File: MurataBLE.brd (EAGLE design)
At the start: 90 x 70 mm, 58 parts, among them CON1 47589-0001, IC2 LPC11U35_QFN33, IC3 NC7SZ00, IC4 AT25DN512C, IC5 AT25XE011, P1 NC, P2 NC, P3 NC, P4 NC, Q1 32.768K/2012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

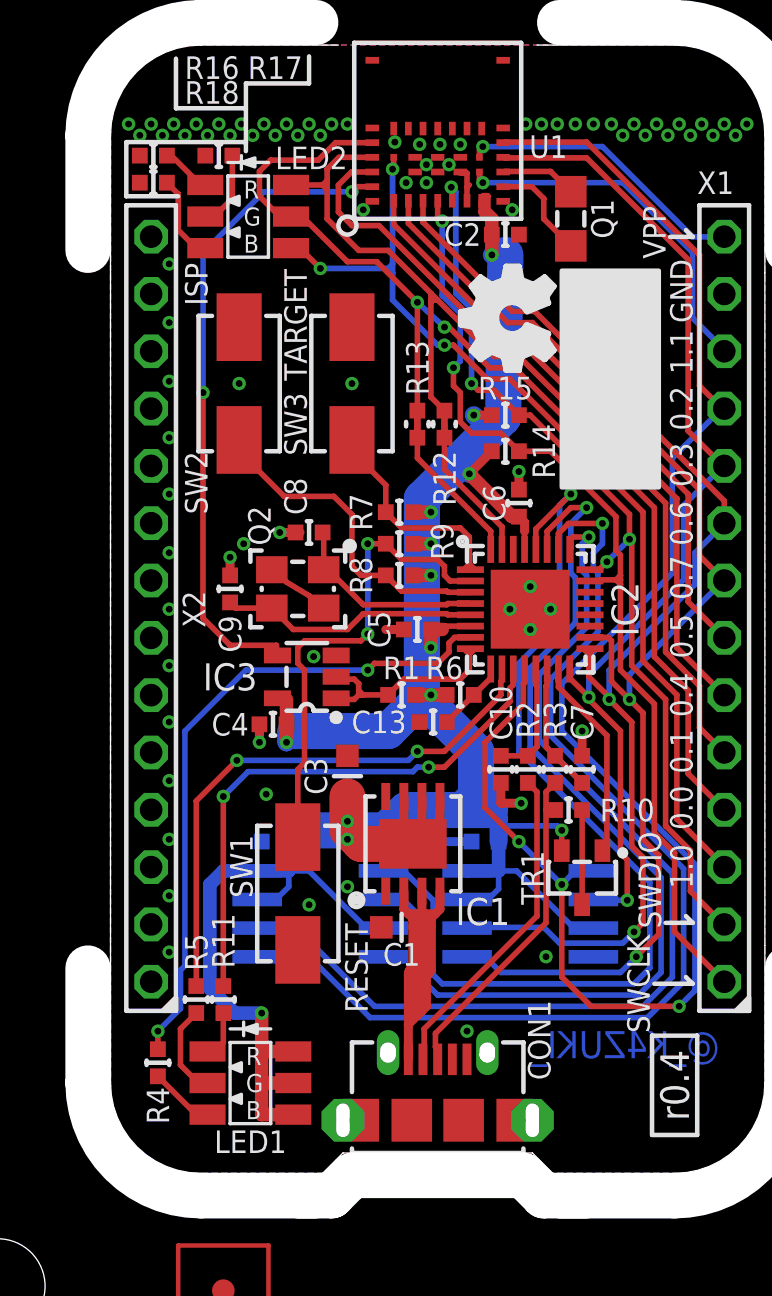
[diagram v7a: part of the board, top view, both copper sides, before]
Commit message: [ USB ] add 3.3V pin; silk; move R4/5/11
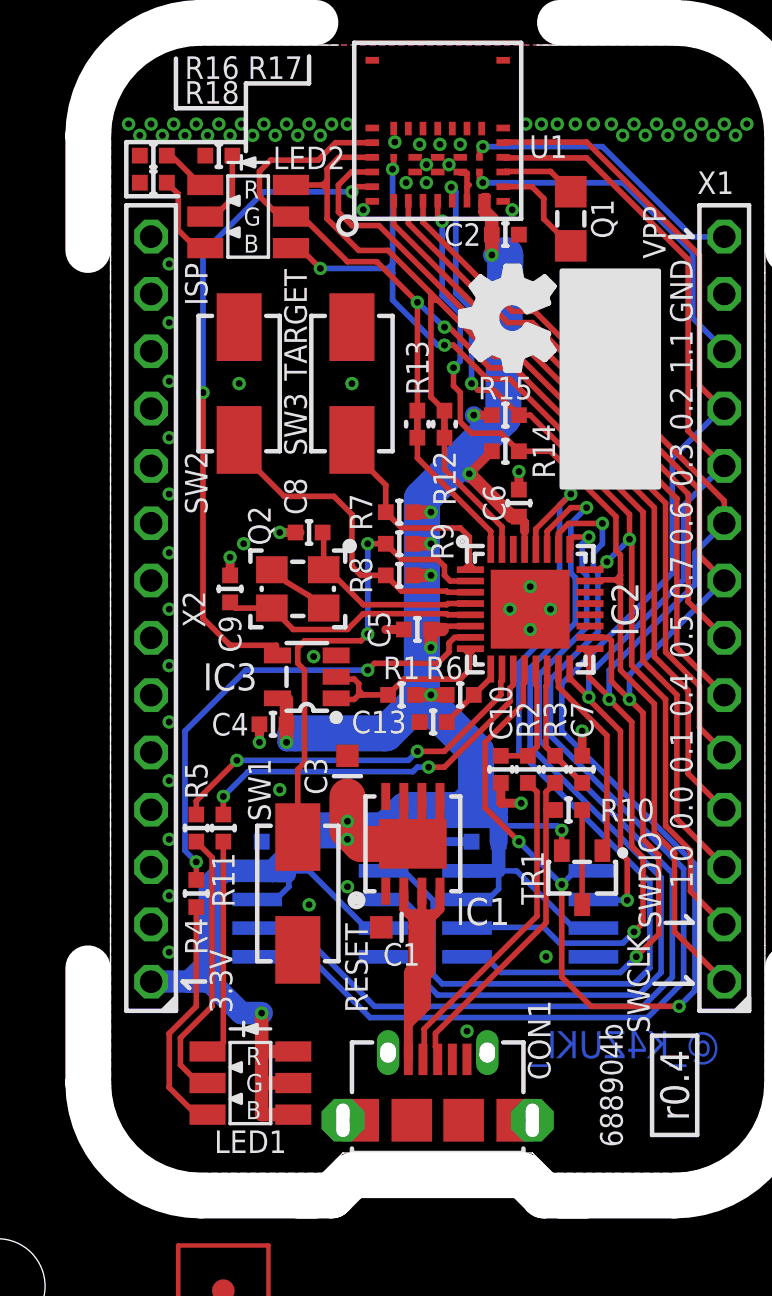
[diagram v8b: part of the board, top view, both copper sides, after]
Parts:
- moved GIT1 35.1 mm to (32.2, 13.9), turned to 90 degrees
- moved R4 7.69 mm to (13.8, 22.4)
- moved R11 7.60 mm to (15.0, 25.3)
- moved R5 7.60 mm to (13.8, 25.3)
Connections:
- net 3.3V: now also X2.1
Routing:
- net N$12: track 4.12 -> 12.3 mm
- net N$13: track 2.90 -> 10.7 mm
- net N$8: track 29.2 -> 21.4 mm
- net N$9: track 24.8 -> 17.2 mm
- net N$11: track 2.17 -> 9.77 mm
- net N$10: track 24.4 -> 16.8 mm
- net 3.3V: track 130.7 -> 136.6 mm
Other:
- board text added: "3.3V"
- board text removed: "C1"
- board text removed: "C10"
- board text removed: "C11"
- board text removed: "C12"
- board text removed: "C13"
- board text removed: "C2"
- board text removed: "C3"
- board text removed: "C4"
- board text removed: "C5"
- board text removed: "C6"
- board text removed: "C7"
- board text removed: "C8"
- board text removed: "C9"
- board text removed: "CON1"
- board text removed: "IC1"
- board text removed: "IC2"
- board text removed: "IC3"
- board text removed: "IC4"
- board text removed: "IC5"
- board text removed: "LED1"
- board text removed: "Q1"
- board text removed: "Q2"
- board text removed: "R1"
- board text removed: "R10"
- board text removed: "R11"
- board text removed: "R12"
- board text removed: "R13"
- board text removed: "R14"
- board text removed: "R15"
- board text removed: "R2"
- board text removed: "R3"
- board text removed: "R4"
- board text removed: "R5"
- board text removed: "R6"
- board text removed: "R7"
- board text removed: "R8"
- board text removed: "R9"
- board text removed: "SW1"
- board text removed: "SW2"
- board text removed: "SW3"
- board text removed: "TR1"
- board text removed: "X1"
- board text removed: "X2"
